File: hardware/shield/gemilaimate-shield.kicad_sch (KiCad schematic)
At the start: 34 parts, among them J1 ISOLATED 5V INPUT, J10 HEATER UNUSED, J2 ADS1115 BLUE SOCKET 1x10, J3 MAX31855 VIN SOCKET 1x6, J4 PRESSURE SENSOR, J5 ROBOTDYN EDGE DOCK 1x4, J6 SSR EDGE DOCK 1x5 USE 1-3-5, J7 CJMCU-0102 SOCKET 2x5, J8 DRY CONTACTS ONLY, J9 DISPLAY USB 5V, U1 ESP32-S3-N8R8 DevKitC-1, U2 SN74AHCT125N PDIP14, U3 SN74LVC1G17DBV SOT23-5

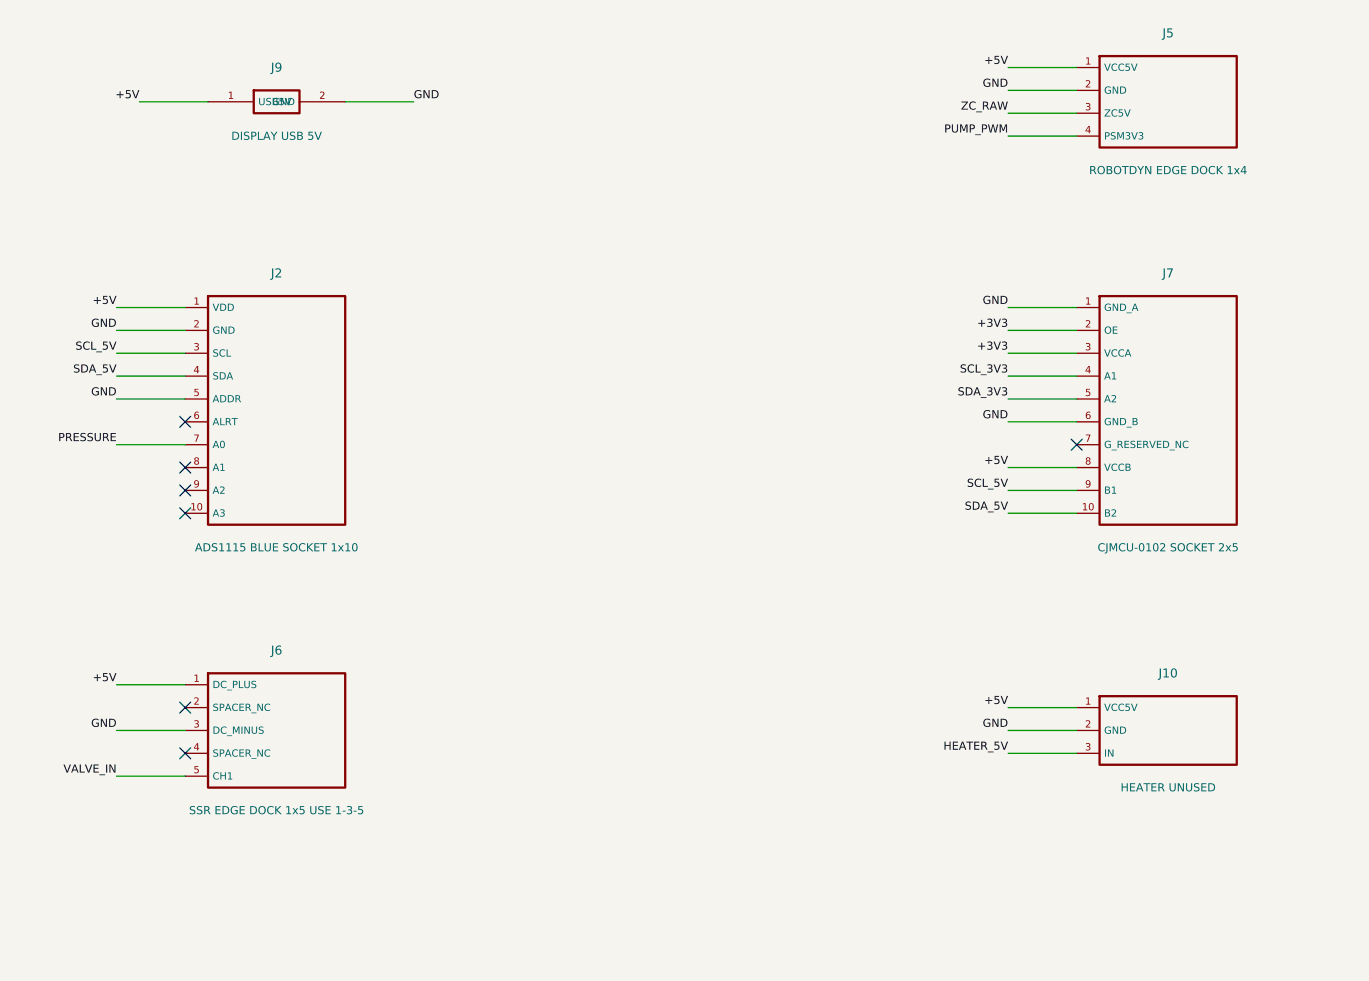
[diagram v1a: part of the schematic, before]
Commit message: Apply shield assembly review and headless rebuild fixes
Revise shield to v0.2.2 with square pin-1 pads, explicit orientation labels and module outlines. Use wired controls for externally mounted RobotDyn and SSR, preserve SSR terminals, reserve mating connector and cable envelopes, move J4 for mounting clearance, and document adjustable module retention. Rebuild on Linux KiCad 10.0.7 without DISPLAY; ERC, DRC, unconnected and parity all zero. Carrier electronics and firmware remain unchanged.
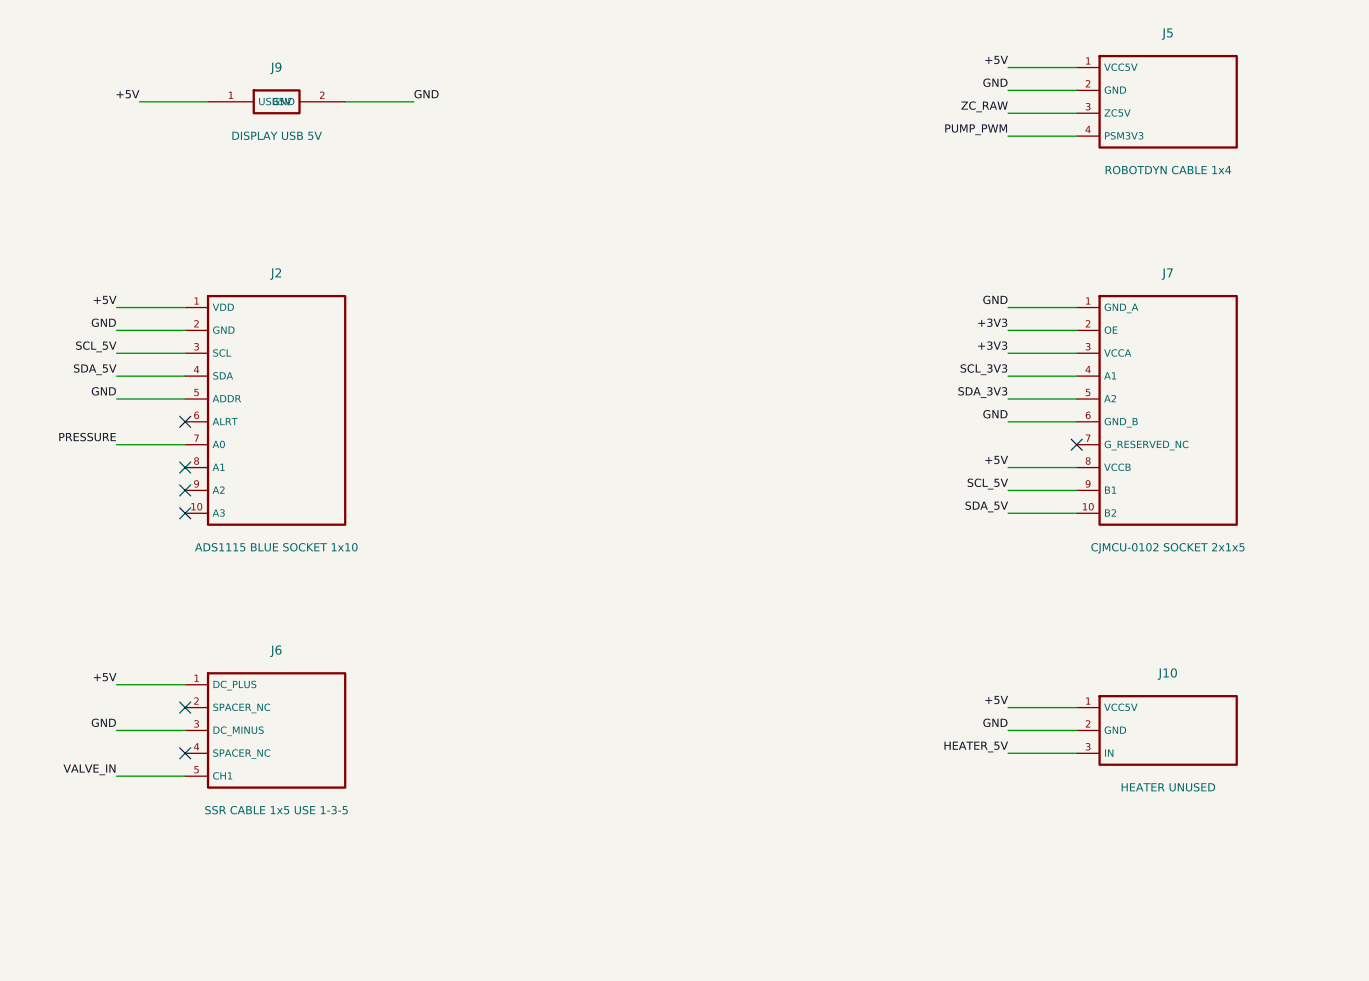
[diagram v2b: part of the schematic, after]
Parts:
- J5: value ROBOTDYN EDGE DOCK 1x4 -> ROBOTDYN CABLE 1x4
- J6: value SSR EDGE DOCK 1x5 USE 1-3-5 -> SSR CABLE 1x5 USE 1-3-5
- J7: value CJMCU-0102 SOCKET 2x5 -> CJMCU-0102 SOCKET 2x1x5
